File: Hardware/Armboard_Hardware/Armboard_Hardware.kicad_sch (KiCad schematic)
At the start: 329 parts, among them J1 RJ45_LED_Shielded, Q1 Si4156DY, Q2 Si4156DY, Q3 Si4156DY, Q4 Si4156DY, Q41 BSS138, Q42 BSS138, Q43 T2N7002AK,LM, Q44 T2N7002AK,LM, Q45 T2N7002AK,LM, Q46 T2N7002AK,LM, Q47 T2N7002AK,LM, Q48 T2N7002AK,LM, Q49 T2N7002AK,LM, Q50 T2N7002AK,LM, Q51 T2N7002AK,LM, Q52 T2N7002AK,LM, Q53 T2N7002AK,LM, Q54 T2N7002AK,LM, Q55 T2N7002AK,LM, Q56 T2N7002AK,LM, Q57 T2N7002AK,LM, Q58 T2N7002AK,LM, Q59 T2N7002AK,LM, Q60 T2N7002AK,LM, Q61 T2N7002AK,LM, Q62 T2N7002AK,LM, Q63 AO3401A, SW1 SW_Push, SW10 SW_SPDT, SW11 SW_Push, SW12 SW_Push, SW2 SW_Push, SW3 SW_Push, SW4 SW_Push, SW5 SW_Push, SW6 SW_Push, SW7 SW_Push, SW8 SW_Push, SW9 SW_Push, U1 74LVC2G04, U1 OKI, U2 IRS2308, U2 Teensy4.1_DEV-16771, U3 74LS148, U3 IRS2308, U36 OKI, U37 PCF8574, U38 PCF8574, U4 74LS148, U5 74HC00

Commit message: Added VNH circuit and IO Expander
Added VNH circuit and IO Expander for VNH pins. Organized Schematic, and changed voltage labels
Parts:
- removed C2 (x20): 10uF, Capacitor_SMD:C_0603_1608Metric_Pad1.08x0.95mm_HandSolder, symbol Device:C
- removed C2 (x10), C4 (x10): 1uF, Capacitor_SMD:C_0603_1608Metric_Pad1.08x0.95mm_HandSolder, symbol Device:C
- removed Conn2 (x10): AndersonPP, MRDT_Connectors:Square_Anderson_2_H_Side_By_Side, symbol MRDT_Connectors:AndersonPP
- removed D2 (x10), D3 (x10): SD0603S04, Diode_SMD:D_0603_1608Metric_Pad1.05x0.95mm_HandSolder, symbol Device:D
- removed D34, D35, D36, D37, D38, D39, D40, D41, D42, D44: Blue, LED_SMD:LED_0603_1608Metric_Pad1.05x0.95mm_HandSolder, symbol Device:LED
- removed Q1 (x10), Q2 (x10), Q3 (x10), Q4 (x10): Si4156DY, Package_SO:SOIC-8_3.9x4.9mm_P1.27mm, symbol Transistor_FET:Si4162DY
- removed Q53, Q54, Q55, Q56, Q57, Q58, Q59, Q60, Q61, Q62: T2N7002AK,LM, Package_TO_SOT_SMD:SOT-23-3, symbol T2N7002AK_LM:T2N7002AK,LM
- removed R2 (x10), R3 (x10), R4 (x10), R5 (x10): 100, Resistor_SMD:R_0603_1608Metric_Pad0.98x0.95mm_HandSolder, symbol Device:R
- removed unit 2 of U1 (x10)
- removed unit 3 of U1 (x10)
- removed U2 (x10), U3 (x10): IRS2308, Package_SO:SOIC-8_3.9x4.9mm_P1.27mm, symbol Driver_FET:IRS2308
- added C1, C11, C13, C14, C17, C18, C21, C29, C7, C9: 0.1uF, symbol Device:C
- added C10, C12, C15, C16, C19, C20, C23, C31, C5, C8: 10nF, symbol Device:C
- added C22, C24, C30: 10 uF, Capacitor_SMD:C_0603_1608Metric_Pad1.08x0.95mm_HandSolder, symbol Device:C
- added Conn10, Conn2, Conn3, Conn34, Conn4, Conn5, Conn6, Conn7, Conn8, Conn9: AndersonPP, symbol MRDT_Connectors:AndersonPP
- added R1, R104, R13, R19, R25, R36, R37, R92: 10k, symbol Device:R
- added R10, R11, R14, R15, R16, R17, R20, R21, R22, R23, R26, R27, R28, R29, R3, R30, R31, R32, R33, R38, R39, R4, R40, R5, R6, R79, R8, R80, R85, R9, R94, R95, R96, R97: 1k, symbol Device:R
- added R102, R12, R18, R2, R24, R34, R35, R90: 330, symbol Device:R
- added U10, U11, U12, U14, U3, U4, U5, U7, U8, U9: VNH7070AS, symbol MRDT_Devices:VNH7070AS
- added U13, U15, U16: PCF8574, Package_SO:SOIC-16W_7.5x10.3mm_P1.27mm, symbol Interface_Expansion:PCF8574
- R65, R66, R67, R68, R69, R75: value 220 -> 1k; footprint Resistor_SMD:R_0603_1608Metric_Pad0.98x0.95mm_HandSolder -> (none)
- R70, R71: value 220 -> 330; footprint Resistor_SMD:R_0603_1608Metric_Pad0.98x0.95mm_HandSolder -> (none)
- R73, R74: value 220 -> 10k; footprint Resistor_SMD:R_0603_1608Metric_Pad0.98x0.95mm_HandSolder -> (none)
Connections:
- net MOTOR4_PWM_RVS is gone; now on net PWM8: U2.4 (BCLK2)
- net MOTOR8_PWM_RVS is gone; now on net SEL6: U2.6 (OUT1D)
- net +12V: now also C1.2, C11.2, C13.2, C14.2, C17.2, C18.2, C21.2, C29.2, C7.2, C9.2, U10.12 (VCC), U10.4 (VCC), U10.5 (VCC), U11.12 (VCC), U11.4 (VCC), U11.5 (VCC), U12.12 (VCC), U12.4 (VCC), U12.5 (VCC), U14.12 (VCC), U14.4 (VCC), U14.5 (VCC), U3.12 (VCC), U3.4 (VCC), U3.5 (VCC), U4.12 (VCC), U4.4 (VCC), U4.5 (VCC), U5.12 (VCC), U5.4 (VCC), U5.5 (VCC), U7.12 (VCC), U7.4 (VCC), U7.5 (VCC), U8.12 (VCC), U8.4 (VCC), U8.5 (VCC), U9.12 (VCC), U9.4 (VCC), U9.5 (VCC)
- net +3V3: now also R43.1, U3.16 (VCC), U4.1 (I4), U4.13 (I3), U4.16 (VCC), U4.2 (I5), U4.3 (I6), U4.4 (I7), U5.14 (VCC), C22.1, C24.1, C30.1, U13.16 (VDD), U13.2 (A1), U15.1 (A0), U15.16 (VDD), U15.2 (A1), U16.16 (VDD), U16.3 (A2)
- net +5V: no longer U2.5V
- net DIR_SW: now also U16.4 (P0); no longer U4.13 (I3)
- net GND: now also R70.2, R71.2, C1.1, C10.2, C11.1, C12.2, C13.1, C14.1, C15.2, C16.2, C17.1, C18.1, C19.2, C20.2, C21.1, C22.2, C23.2, C24.2, C29.1, C30.2, C31.2, C5.2, C7.1, C8.2, C9.1, R102.2, R12.2, R18.2, R2.2, R24.2, R34.2, R35.2, R90.2, U10.1 (GND_A), U10.16 (GND_A), U10.8 (GND_B), U10.9 (GND_B), U11.1 (GND_A), U11.16 (GND_A), U11.8 (GND_B), U11.9 (GND_B), U12.1 (GND_A), U12.16 (GND_A), U12.8 (GND_B), U12.9 (GND_B), U13.1 (A0), U13.3 (A2), U13.8 (VSS), U14.1 (GND_A), U14.16 (GND_A), U14.8 (GND_B), U14.9 (GND_B), U15.3 (A2), U15.8 (VSS), U16.1 (A0), U16.2 (A1), U16.8 (VSS), U3.1 (GND_A), U3.16 (GND_A), U3.8 (GND_B), U3.9 (GND_B), U4.1 (GND_A), U4.16 (GND_A), U4.8 (GND_B), U4.9 (GND_B), U5.1 (GND_A), U5.16 (GND_A), U5.8 (GND_B), U5.9 (GND_B), U7.1 (GND_A), U7.16 (GND_A), U7.8 (GND_B), U7.9 (GND_B), U8.1 (GND_A), U8.16 (GND_A), U8.8 (GND_B), U8.9 (GND_B), U9.1 (GND_A), U9.16 (GND_A), U9.8 (GND_B), U9.9 (GND_B)
- net SCL: now also U13.14 (SCL), U15.14 (SCL), U16.14 (SCL)
- net SDA: now also U13.15 (SDA), U15.15 (SDA), U16.15 (SDA)
- net PWM8: now reaches R68.1
- net PWM8: now also Q50.1 (G)
- net PWM9: now reaches U2.33 (MCLK2)
- net PWM9: now also Q51.1 (G), R80.1
- net IN_B8: now reaches R67.1
- net IN_B8: now also U15.9 (P4)
- net at R71.1: now also R74.1, U11.13 (CS)
- net CS1: now reaches R74.2
- net CS1: now also R73.2, U2.17 (A3), C10.1, C12.1, C15.1, C16.1, C19.1, C20.1, C23.1, C31.1, C5.1, C8.1, R1.2, R104.2, R13.2, R19.2, R25.2, R36.2, R37.2, R92.2
- net IN_A9: now reaches R75.1
- net IN_A9: now also U15.10 (P5)
- net at R75.2: now also U12.3 (IN_A)
- net at R70.1: now also R73.1, U10.13 (CS)
- net SEL8: now reaches R69.1
- net SEL8: now also U2.12 (MISO)
- net at R69.2: now also U11.14 (SEL)
- net at R68.2: now also U11.11 (PWM)
- net IN_A1: now reaches U38.10 (P5)
- net IN_A1: now also R5.1
- net IN_B1: now reaches U38.11 (P6)
- net IN_B1: now also R6.1
- net IN_A2: now reaches U38.12 (P7)
- net IN_A2: now also R8.1
- net SEL10: now reaches U38.9 (P4)
- net SEL10: now also R97.1
- net at R67.2: now also U11.6 (IN_B)
- net at R65.2: now also U10.14 (SEL)
- net at R66.2: now also U11.3 (IN_A)
- net SEL6: now reaches R65.1
- net IN_A8: now reaches R66.1
- net IN_A8: now also U15.7 (P3)
- removed net +3.3V: R43.1, U2.3.3V_1 (3.3V), U2.3.3V_2 (3.3V), U2.3.3V_3 (3.3V), U3.16 (VCC), U4.1 (I4), U4.16 (VCC), U4.2 (I5), U4.3 (I6), U4.4 (I7), U5.14 (VCC)
- net MOTOR10_PWM_FWD renamed PWM10
- net PWM10: now also U2.13 (SCK), R96.1; no longer U2.12 (MISO)
- net MOTOR10_PWM_RVS renamed SEL9
- net SEL9: now also R85.1
- net MOTOR1_PWM_FWD renamed PWM1
- net PWM1: now also R3.1
- net MOTOR1_PWM_RVS renamed PWM2
- net PWM2: now also Q44.1 (G), R10.1
- net MOTOR2_PWM_FWD renamed PWM3
- net PWM3: now also Q45.1 (G), R16.1; no longer Q44.1 (G)
- net MOTOR2_PWM_RVS renamed PWM4
- net PWM4: now also Q46.1 (G), R22.1
- net MOTOR3_PWM_FWD renamed PWM5
- net PWM5: now also Q47.1 (G), R28.1; no longer Q45.1 (G)
- net MOTOR3_PWM_RVS renamed PWM6
- net PWM6: now also Q48.1 (G), R40.1
- net MOTOR4_PWM_FWD renamed PWM7
- net PWM7: now also Q49.1 (G), R32.1; no longer Q46.1 (G)
- removed net MOTOR5_PWM_FWD: Q47.1 (G), U2.13 (SCK)
- net MOTOR5_PWM_RVS renamed SEL1
- net SEL1: now also R4.1
- net MOTOR6_PWM_FWD renamed SEL2
- net SEL2: now also R11.1; no longer Q48.1 (G)
- net MOTOR6_PWM_RVS renamed SEL3
- net SEL3: now also R17.1
- removed net MOTOR7_PWM_FWD: Q49.1 (G), U2.17 (A3)
- net MOTOR7_PWM_RVS renamed SEL4
- net SEL4: now also R23.1
- net MOTOR8_PWM_FWD renamed SEL5
- net SEL5: now also R29.1; no longer Q50.1 (G)
- net MOTOR9_PWM_FWD renamed SEL7
- net SEL7: now also R33.1; no longer Q51.1 (G)
- net MOTOR9_PWM_RVS: no longer names the net of U2.10 (CS1)
- new net: Conn6.1 (GND), U8.10 (OUT_B), U8.7 (OUT_B)
- new net: R21.2, U7.6 (IN_B)
- new net: R10.2, U4.11 (PWM)
- new net: Conn2.1 (GND), U3.10 (OUT_B), U3.7 (OUT_B)
- new net: R3.2, U3.11 (PWM)
- new net: R1.1, R2.1, U3.13 (CS)
- new net: R4.2, U3.14 (SEL)
- new net: Conn2.2 (V+Log), U3.15 (OUT_A), U3.2 (OUT_A)
- new net: R5.2, U3.3 (IN_A)
- new net: R6.2, U3.6 (IN_B)
- new net: R18.1, R19.1, U5.13 (CS)
- new net: U2.3.3V_1 (3.3V), U2.3.3V_2 (3.3V), U2.3.3V_3 (3.3V)
- new net: R20.2, U7.3 (IN_A)
- new net: Conn34.1 (GND), U14.10 (OUT_B), U14.7 (OUT_B)
- new net: Conn8.1 (GND), U10.10 (OUT_B), U10.7 (OUT_B)
- new net: R31.2, U9.6 (IN_B)
- new net: Conn10.1 (GND), U12.10 (OUT_B), U12.7 (OUT_B)
- new net: R80.2, U12.11 (PWM)
- new net: R90.1, R92.1, U12.13 (CS)
- new net: R85.2, U12.14 (SEL)
- new net: Conn10.2 (V+Log), U12.15 (OUT_A), U12.2 (OUT_A)
- new net: R79.2, U12.6 (IN_B)
- new net: R28.2, U8.11 (PWM)
- new net: R34.1, R36.1, U8.13 (CS)
- new net: R29.2, U8.14 (SEL)
- new net: Conn6.2 (V+Log), U8.15 (OUT_A), U8.2 (OUT_A)
- new net: R26.2, U8.3 (IN_A)
- new net: R27.2, U8.6 (IN_B)
- new net: R102.1, R104.1, U14.13 (CS)
- new net: R17.2, U5.14 (SEL)
- new net: R15.2, U5.6 (IN_B)
- new net: R12.1, R13.1, U4.13 (CS)
- new net: Conn5.1 (GND), U7.10 (OUT_B), U7.7 (OUT_B)
- new net: R22.2, U7.11 (PWM)
- new net: R24.1, R25.1, U7.13 (CS)
- new net: R23.2, U7.14 (SEL)
- new net: Conn5.2 (V+Log), U7.15 (OUT_A), U7.2 (OUT_A)
- new net: Conn3.1 (GND), U4.10 (OUT_B), U4.7 (OUT_B)
- new net: R39.2, U10.6 (IN_B)
- new net: R11.2, U4.14 (SEL)
- new net: Conn4.2 (V+Log), U5.15 (OUT_A), U5.2 (OUT_A)
- new net: R95.2, U14.6 (IN_B)
- new net: Conn9.1 (GND), U11.10 (OUT_B), U11.7 (OUT_B)
- new net: Conn9.2 (V+Log), U11.15 (OUT_A), U11.2 (OUT_A)
- new net: R8.2, U4.3 (IN_A)
- new net: R96.2, U14.11 (PWM)
- new net: R97.2, U14.14 (SEL)
- new net: Conn34.2 (V+Log), U14.15 (OUT_A), U14.2 (OUT_A)
- new net: R94.2, U14.3 (IN_A)
- new net: R40.2, U10.11 (PWM)
- new net: R16.2, U5.11 (PWM)
- new net: Conn8.2 (V+Log), U10.15 (OUT_A), U10.2 (OUT_A)
- new net: R38.2, U10.3 (IN_A)
- new net: Conn4.1 (GND), U5.10 (OUT_B), U5.7 (OUT_B)
- new net: R14.2, U5.3 (IN_A)
- new net: R35.1, R37.1, U9.13 (CS)
- new net: Conn3.2 (V+Log), U4.15 (OUT_A), U4.2 (OUT_A)
- new net: R9.2, U4.6 (IN_B)
- new net: R32.2, U9.11 (PWM)
- new net: R33.2, U9.14 (SEL)
- new net: Conn7.1 (GND), U9.10 (OUT_B), U9.7 (OUT_B)
- new net: Conn7.2 (V+Log), U9.15 (OUT_A), U9.2 (OUT_A)
- new net: R30.2, U9.3 (IN_A)
- new net IN_A10: R94.1, U15.12 (P7)
- new net IN_A3: R14.1, U13.5 (P1)
- new net IN_A4: R20.1, U13.7 (P3)
- new net IN_A5: R26.1, U13.10 (P5)
- new net IN_A6: R38.1, U13.12 (P7)
- new net IN_A7: R30.1, U15.5 (P1)
- new net IN_B10: R95.1, U16.5 (P1)
- new net IN_B2: R9.1, U13.4 (P0)
- new net IN_B3: R15.1, U13.6 (P2)
- new net IN_B4: R21.1, U13.9 (P4)
- new net IN_B5: R27.1, U13.11 (P6)
- new net IN_B6: R39.1, U15.4 (P0)
- new net IN_B7: R31.1, U15.6 (P2)
- new net IN_B9: R79.1, U15.11 (P6)
- no-connect marks 16 -> 24
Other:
- note added: "VNH Drive LEDs"
- note added: "VNH Drivers"
- note removed: "H-Bridge Drivers"
- note removed: "H-Bridge LED FWD"
- note removed: "H-Bridge LED RVS"
- note removed: "Inverter Power"
- moved on the sheet: C26, C27, C28, C48, C49, C50, Conn1A, Conn1B, D1, D10, D11, D2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

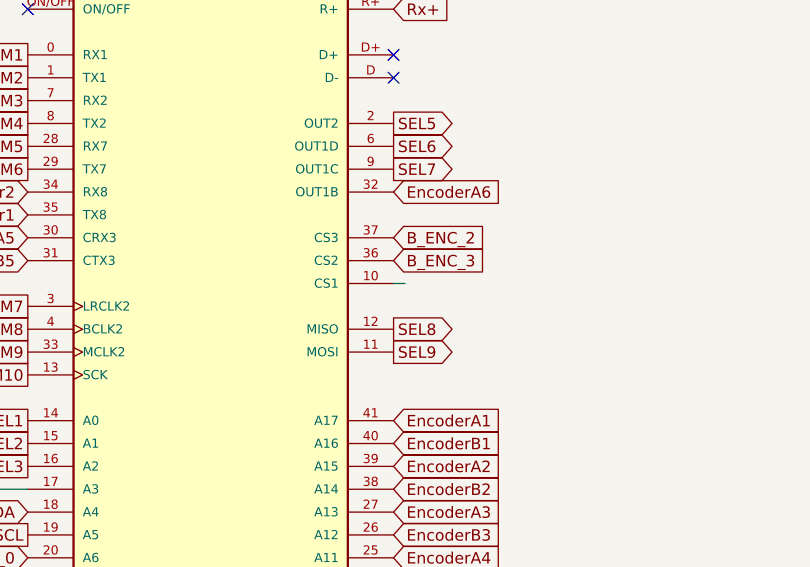
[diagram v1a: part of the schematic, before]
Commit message: Completed Footprint Assignment
Completed Footprint Assignment
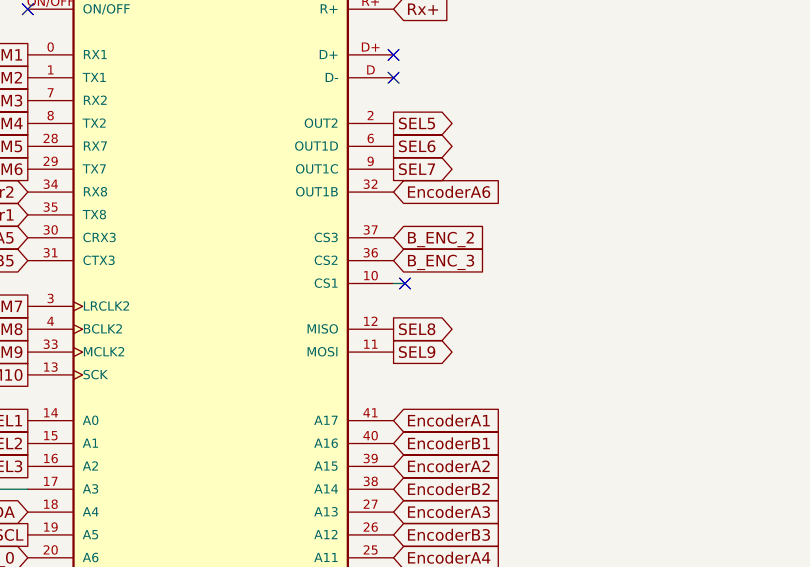
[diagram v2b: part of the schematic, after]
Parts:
- C1, C10, C11, C12, C13, C14, C15, C16, C17, C18, C19, C20, C21, C23, C29, C31, C5, C7, C8, C9: footprint (none) -> Capacitor_SMD:C_0603_1608Metric_Pad1.08x0.95mm_HandSolder
- Conn10, Conn2, Conn3, Conn34, Conn4, Conn5, Conn6, Conn7, Conn8, Conn9: footprint (none) -> MRDT_Connectors:Anderson_1_Horizontal
- R1, R10, R102, R104, R11, R12, R13, R14, R15, R16, R17, R18, R19, R2, R20, R21, R22, R23, R24, R25, R26, R27, R28, R29, R3, R30, R31, R32, R33, R34, R35, R36, R37, R38, R39, R4, R40, R5, R6, R65, R66, R67, R68, R69, R70, R71, R73, R74, R75, R79, R8, R80, R85, R9, R90, R92, R94, R95, R96, R97: footprint (none) -> Resistor_SMD:R_0603_1608Metric_Pad0.98x0.95mm_HandSolder
- U10, U11, U12, U14, U3, U4, U5, U7, U8, U9: footprint (none) -> Package_SO:SOIC-16_3.9x9.9mm_P1.27mm
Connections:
- no-connect marks 24 -> 25

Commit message: Placed Components and Made Power Planes
Placed Components for trace routing, and made power planes for motors and 12V
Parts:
- Conn10, Conn2, Conn3, Conn34, Conn4, Conn5, Conn6, Conn7, Conn8, Conn9: footprint MRDT_Connectors:Anderson_1_Horizontal -> MRDT_Connectors:Square_Anderson_2_H_Side_By_Side
- U3, U4: footprint Package_SO:SOIC-16_3.9x9.9mm_P1.27mm -> Package_SO:SOIC-16W_7.5x10.3mm_P1.27mm
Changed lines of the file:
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@@
       (effects (font (size 1.524 1.524)) (justify right))
     )
-    (property "Footprint" "MRDT_Connectors:Anderson_1_Horizontal" (at 188.595 527.05 0)
+    (property "Footprint" "MRDT_Connectors:Square_Anderson_2_H_Side_By_Side" (at 188.595 527.05 0)
       (effects (font (size 1.524 1.524)) hide)
     )
@@
       (effects (font (size 1.524 1.524)) (justify right))
     )
-    (property "Footprint" "MRDT_Connectors:Anderson_1_Horizontal" (at 292.1 709.93 0)
+    (property "Footprint" "MRDT_Connectors:Square_Anderson_2_H_Side_By_Side" (at 292.1 709.93 0)
       (effects (font (size 1.524 1.524)) hide)
     )
@@
       (effects (font (size 1.524 1.524)) (justify right))
     )
-    (property "Footprint" "MRDT_Connectors:Anderson_1_Horizontal" (at 290.195 526.415 0)
+    (property "Footprint" "MRDT_Connectors:Square_Anderson_2_H_Side_By_Side" (at 290.195 526.415 0)
       (effects (font (size 1.524 1.524)) hide)
     )
@@
       (effects (font (size 1.27 1.27)))
     )
-    (property "Footprint" "Package_SO:SOIC-16_3.9x9.9mm_P1.27mm" (at 760.73 309.88 0)
+    (property "Footprint" "Package_SO:SOIC-16W_7.5x10.3mm_P1.27mm" (at 760.73 309.88 0)
       (effects (font (size 1.27 1.27)) hide)
     )
@@
       (effects (font (size 1.524 1.524)) (justify right))
     )
-    (property "Footprint" "MRDT_Connectors:Anderson_1_Horizontal" (at 290.83 363.855 0)
+    (property "Footprint" "MRDT_Connectors:Square_Anderson_2_H_Side_By_Side" (at 290.83 363.855 0)
       (effects (font (size 1.524 1.524)) hide)
     )
@@
       (effects (font (size 1.524 1.524)) (justify right))
     )
-    (property "Footprint" "MRDT_Connectors:Anderson_1_Horizontal" (at 187.96 438.15 0)
+    (property "Footprint" "MRDT_Connectors:Square_Anderson_2_H_Side_By_Side" (at 187.96 438.15 0)
       (effects (font (size 1.524 1.524)) hide)
     )
@@
       (effects (font (size 1.524 1.524)) (justify right))
     )
-    (property "Footprint" "MRDT_Connectors:Anderson_1_Horizontal" (at 189.23 358.775 0)
+    (property "Footprint" "MRDT_Connectors:Square_Anderson_2_H_Side_By_Side" (at 189.23 358.775 0)
       (effects (font (size 1.524 1.524)) hide)
     )
@@
       (effects (font (size 1.524 1.524)) (justify right))
     )
-    (property "Footprint" "MRDT_Connectors:Anderson_1_Horizontal" (at 289.56 437.515 0)
+    (property "Footprint" "MRDT_Connectors:Square_Anderson_2_H_Side_By_Side" (at 289.56 437.515 0)
       (effects (font (size 1.524 1.524)) hide)
     )
@@
       (effects (font (size 1.524 1.524)) (justify right))
     )
-    (property "Footprint" "MRDT_Connectors:Anderson_1_Horizontal" (at 190.5 710.565 0)
+    (property "Footprint" "MRDT_Connectors:Square_Anderson_2_H_Side_By_Side" (at 190.5 710.565 0)
       (effects (font (size 1.524 1.524)) hide)
     )
@@
       (effects (font (size 1.524 1.524)) (justify right))
     )
-    (property "Footprint" "MRDT_Connectors:Anderson_1_Horizontal" (at 290.195 520.7 0)
+    (property "Footprint" "MRDT_Connectors:Square_Anderson_2_H_Side_By_Side" (at 290.195 520.7 0)
       (effects (font (size 1.524 1.524)) hide)
     )
@@
       (effects (font (size 1.524 1.524)) (justify right))
     )
-    (property "Footprint" "MRDT_Connectors:Anderson_1_Horizontal" (at 189.23 364.49 0)
+    (property "Footprint" "MRDT_Connectors:Square_Anderson_2_H_Side_By_Side" (at 189.23 364.49 0)
       (effects (font (size 1.524 1.524)) hide)
     )
@@
       (effects (font (size 1.524 1.524)) (justify right))
     )
-    (property "Footprint" "MRDT_Connectors:Anderson_1_Horizontal" (at 187.96 443.865 0)
+    (property "Footprint" "MRDT_Connectors:Square_Anderson_2_H_Side_By_Side" (at 187.96 443.865 0)
       (effects (font (size 1.524 1.524)) hide)
     )
@@
       (effects (font (size 1.27 1.27)))
     )
-    (property "Footprint" "Package_SO:SOIC-16_3.9x9.9mm_P1.27mm" (at 805.18 309.88 0)
+    (property "Footprint" "Package_SO:SOIC-16W_7.5x10.3mm_P1.27mm" (at 805.18 309.88 0)
       (effects (font (size 1.27 1.27)) hide)
     )
@@
       (effects (font (size 1.524 1.524)) (justify right))
     )
-    (property "Footprint" "MRDT_Connectors:Anderson_1_Horizontal" (at 292.735 603.25 0)
+    (property "Footprint" "MRDT_Connectors:Square_Anderson_2_H_Side_By_Side" (at 292.735 603.25 0)
       (effects (font (size 1.524 1.524)) hide)
     )
@@
       (effects (font (size 1.524 1.524)) (justify right))
     )
-    (property "Footprint" "MRDT_Connectors:Anderson_1_Horizontal" (at 290.83 358.14 0)
+    (property "Footprint" "MRDT_Connectors:Square_Anderson_2_H_Side_By_Side" (at 290.83 358.14 0)
       (effects (font (size 1.524 1.524)) hide)
     )
@@
       (effects (font (size 1.524 1.524)) (justify right))
     )
-    (property "Footprint" "MRDT_Connectors:Anderson_1_Horizontal" (at 190.5 704.85 0)
+    (property "Footprint" "MRDT_Connectors:Square_Anderson_2_H_Side_By_Side" (at 190.5 704.85 0)
       (effects (font (size 1.524 1.524)) hide)
     )
@@
       (effects (font (size 1.524 1.524)) (justify right))
     )
-    (property "Footprint" "MRDT_Connectors:Anderson_1_Horizontal" (at 292.735 608.965 0)
+    (property "Footprint" "MRDT_Connectors:Square_Anderson_2_H_Side_By_Side" (at 292.735 608.965 0)
       (effects (font (size 1.524 1.524)) hide)
     )
@@
       (effects (font (size 1.524 1.524)) (justify right))
     )
-    (property "Footprint" "MRDT_Connectors:Anderson_1_Horizontal" (at 191.135 603.885 0)
+    (property "Footprint" "MRDT_Connectors:Square_Anderson_2_H_Side_By_Side" (at 191.135 603.885 0)
       (effects (font (size 1.524 1.524)) hide)
     )
@@
       (effects (font (size 1.524 1.524)) (justify right))
     )
-    (property "Footprint" "MRDT_Connectors:Anderson_1_Horizontal" (at 191.135 609.6 0)
+    (property "Footprint" "MRDT_Connectors:Square_Anderson_2_H_Side_By_Side" (at 191.135 609.6 0)
       (effects (font (size 1.524 1.524)) hide)
     )
@@
       (effects (font (size 1.524 1.524)) (justify right))
     )
-    (property "Footprint" "MRDT_Connectors:Anderson_1_Horizontal" (at 188.595 521.335 0)
+    (property "Footprint" "MRDT_Connectors:Square_Anderson_2_H_Side_By_Side" (at 188.595 521.335 0)
       (effects (font (size 1.524 1.524)) hide)
     )
@@
       (effects (font (size 1.524 1.524)) (justify right))
     )
-    (property "Footprint" "MRDT_Connectors:Anderson_1_Horizontal" (at 292.1 704.215 0)
+    (property "Footprint" "MRDT_Connectors:Square_Anderson_2_H_Side_By_Side" (at 292.1 704.215 0)
       (effects (font (size 1.524 1.524)) hide)
     )
@@
       (effects (font (size 1.524 1.524)) (justify right))
     )
-    (property "Footprint" "MRDT_Connectors:Anderson_1_Horizontal" (at 289.56 443.23 0)
+    (property "Footprint" "MRDT_Connectors:Square_Anderson_2_H_Side_By_Side" (at 289.56 443.23 0)
       (effects (font (size 1.524 1.524)) hide)
     )

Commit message: Reworked Motor Placement
Moved motor placement to distribute andersons
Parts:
- added C32, C33, C34, C35, C36, C37, C38, C39, C40, C41: 270uF, Capacitor_SMD:C_0603_1608Metric_Pad1.08x0.95mm_HandSolder, symbol Device:C
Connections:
- net +12V: now also C32.2, C33.2, C34.2, C35.2, C36.2, C37.2, C38.2, C39.2, C40.2, C41.2
- net GND: now also C32.1, C33.1, C34.1, C35.1, C36.1, C37.1, C38.1, C39.1, C40.1, C41.1
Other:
- moved on the sheet: C1, C11, C13, C14, C17, C18, C21, C29, C7, C9
